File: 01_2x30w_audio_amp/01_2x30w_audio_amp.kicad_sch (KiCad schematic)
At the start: 20 parts, among them J101 CUI 5.08mm, J102 SSQ-107-03-T-D, J103 SSQ-120-03-T-D, J104 CUI 5.08mm, J105 CUI 5.08mm, J108 CUI 5.08mm, J109 CUI 5.08mm, Q101 AON7534, U101 MCP1416

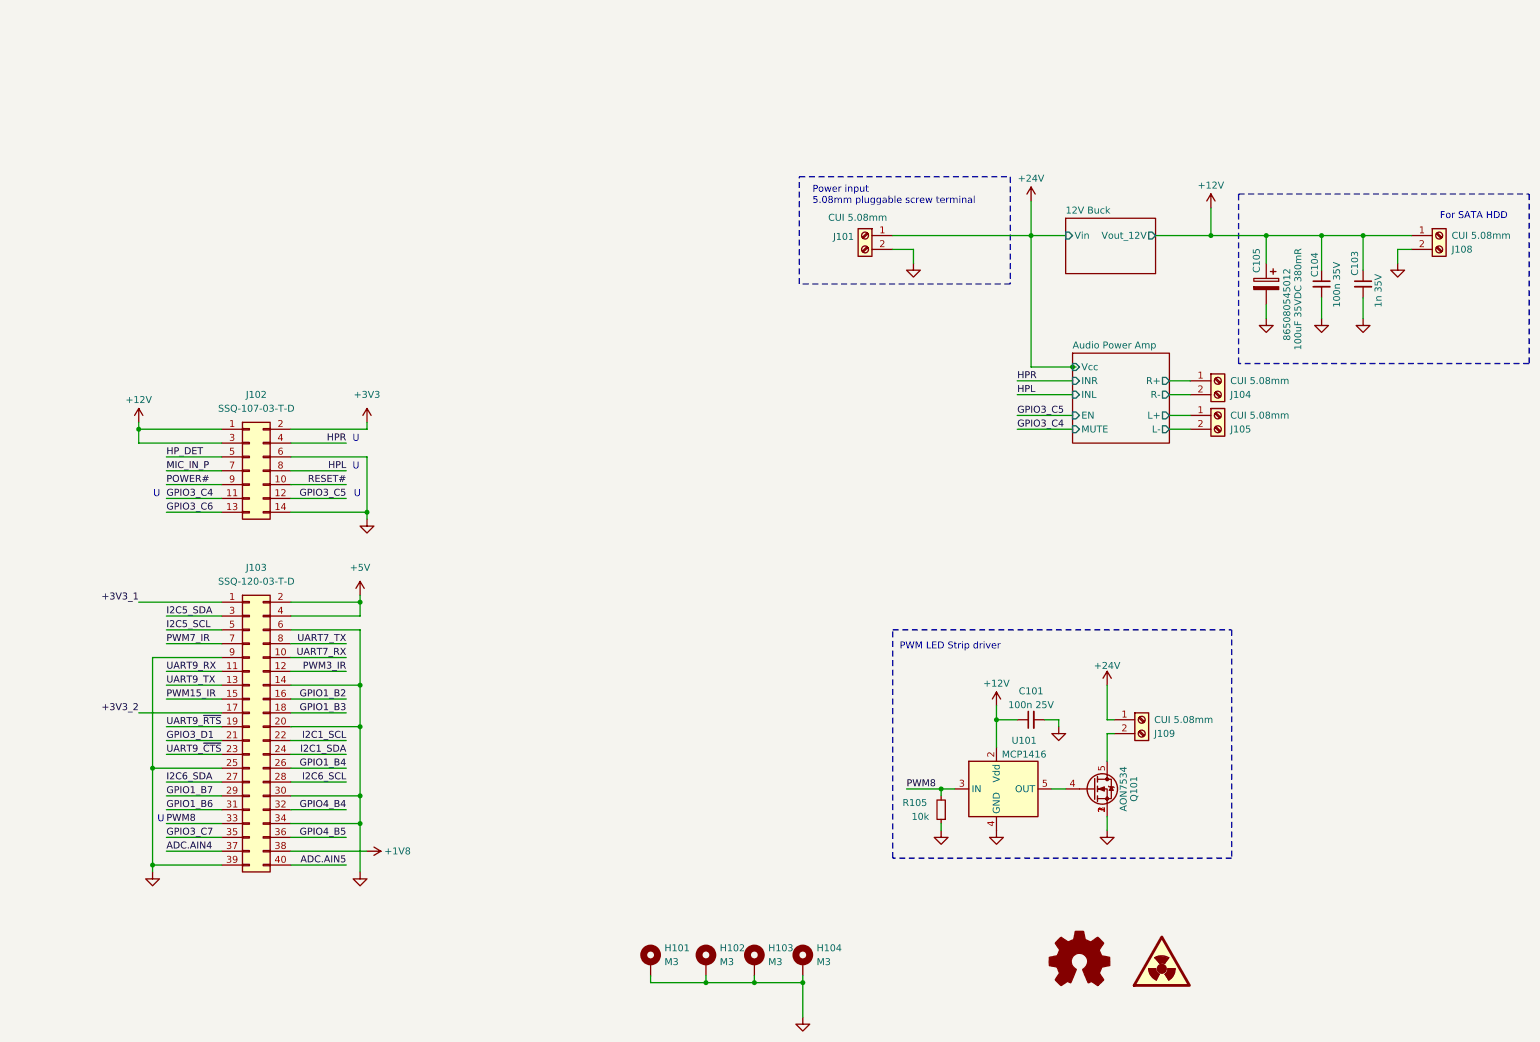
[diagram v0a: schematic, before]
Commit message: Module no. 1 completely redesigned
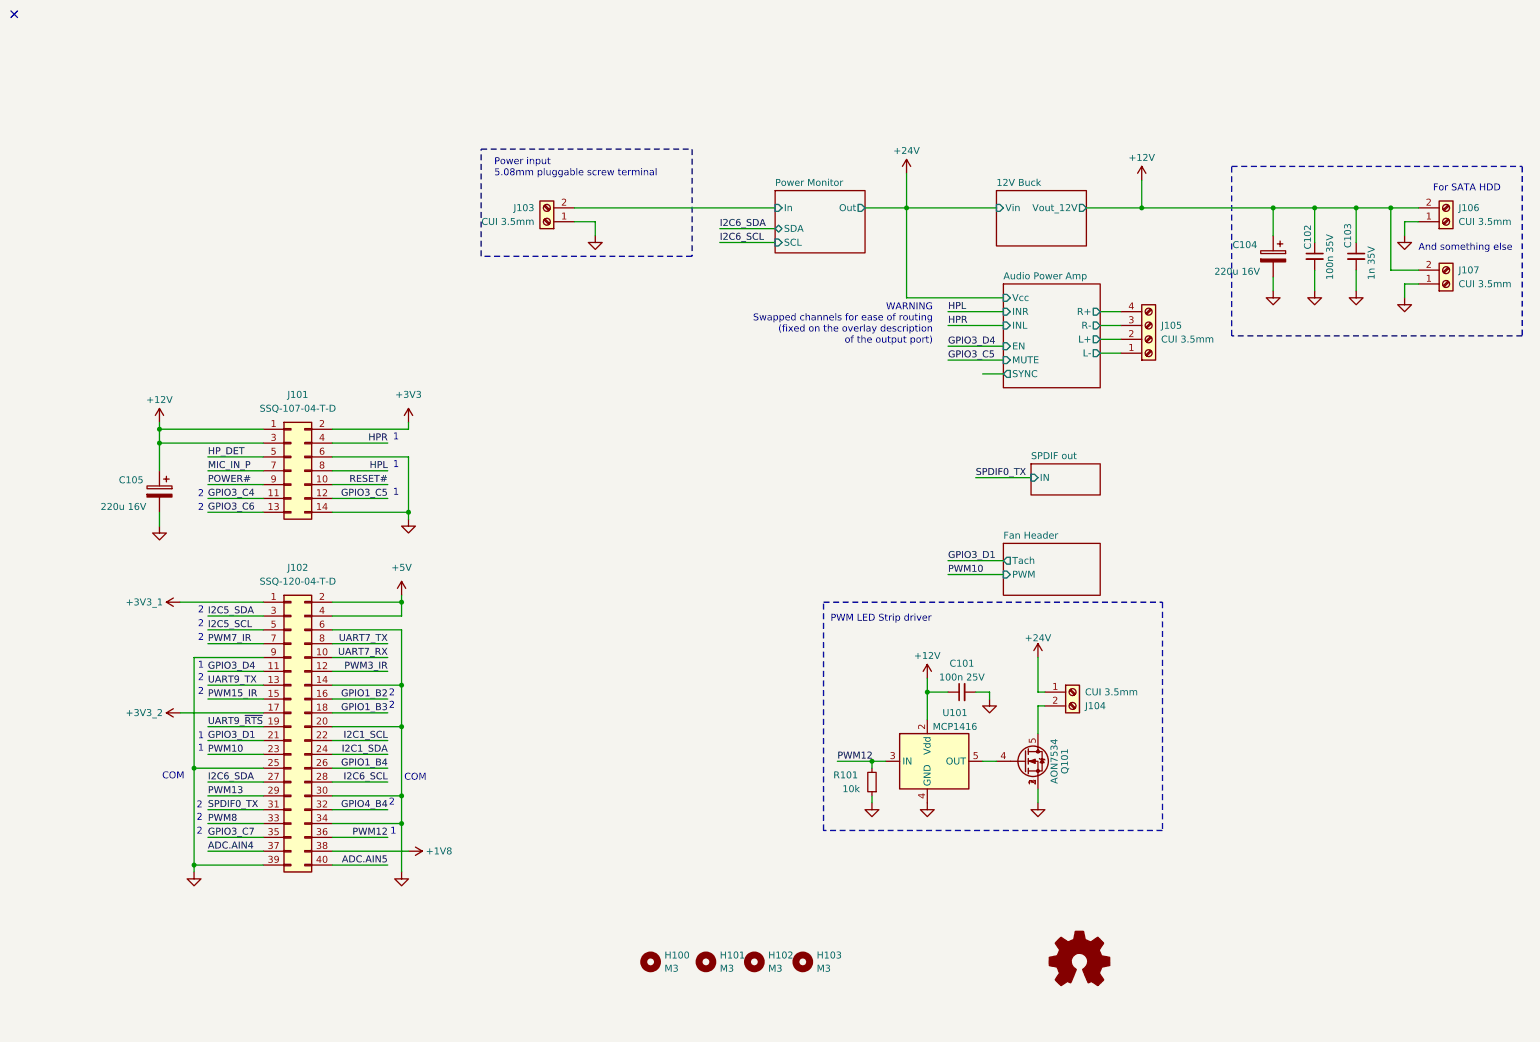
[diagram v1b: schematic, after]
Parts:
- removed J101, J105, J109: CUI 5.08mm, libs:CUI_TBP01R1-508-02BE, symbol Connector:Screw_Terminal_01x02
- removed SYM102: SYM_Radioactive_Large, Symbol:Symbol_Attention_Triangle_8x7mm_Copper, symbol Graphic:SYM_Radioactive_Large
- added C104: A750EK227M1CAAE016, Capacitor_THT:CP_Radial_D6.3mm_P2.50mm, symbol Device:C_Polarized
- added J103, J104, J107: CUI 3.5mm, libs:CUI_TBP03R1-350-02BE, symbol Connector:Screw_Terminal_01x02
- C105: value 865080545012 -> A750EK227M1CAAE016; footprint Capacitor_SMD:C_Elec_6.3x7.7 -> Capacitor_THT:CP_Radial_D6.3mm_P2.50mm
- H100: renamed from H101; footprint MountingHole:MountingHole_3.2mm_M3_DIN965_Pad -> MountingHole:MountingHole_3.2mm_M3_DIN965_Pad_TopBottom; symbol Mechanical:MountingHole_Pad -> Mechanical:MountingHole
- H101: renamed from H102; footprint MountingHole:MountingHole_3.2mm_M3_DIN965_Pad -> MountingHole:MountingHole_3.2mm_M3_DIN965_Pad_TopBottom; symbol Mechanical:MountingHole_Pad -> Mechanical:MountingHole
- H102: renamed from H103; footprint MountingHole:MountingHole_3.2mm_M3_DIN965_Pad -> MountingHole:MountingHole_3.2mm_M3_DIN965_Pad_TopBottom; symbol Mechanical:MountingHole_Pad -> Mechanical:MountingHole
- H103: renamed from H104; footprint MountingHole:MountingHole_3.2mm_M3_DIN965_Pad -> MountingHole:MountingHole_3.2mm_M3_DIN965_Pad_TopBottom; symbol Mechanical:MountingHole_Pad -> Mechanical:MountingHole
- J101: renamed from J102; value SSQ-107-03-T-D -> SSQ-107-04-T-D
- J102: renamed from J103; value SSQ-120-03-T-D -> SSQ-120-04-T-D
- J105: renamed from J104; value CUI 5.08mm -> CUI 3.5mm; footprint libs:CUI_TBP01R1-508-02BE -> libs:CUI_TBP03R1-350-04BE; symbol Connector:Screw_Terminal_01x02 -> Connector:Screw_Terminal_01x04
- J106: renamed from J108; value CUI 5.08mm -> CUI 3.5mm; footprint libs:CUI_TBP01R1-508-02BE -> libs:CUI_TBP03R1-350-02BE
- renumbered C104 to C102, R105 to R101
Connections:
- net +12V: now also J106.2 (Pin_2), C104.1, J107.2 (Pin_2); no longer J106.1 (Pin_1)
- net +24V: now also J104.1 (Pin_1)
- net Audio Power Amp/L+: now also J105.2 (Pin_2)
- net Audio Power Amp/L-: now also J105.1 (Pin_1)
- net Audio Power Amp/R+: now also J105.4 (Pin_4); no longer J105.1 (Pin_1)
- net Audio Power Amp/R-: now also J105.3 (Pin_3); no longer J105.2 (Pin_2)
- net GND: now also J106.1 (Pin_1), C104.2, J103.1 (Pin_1), J107.1 (Pin_1); no longer H100.1, H101.1, H102.1, H103.1, J106.2 (Pin_2)
- net PWM8: no longer R101.2, U101.3 (IN)
- net at Q101.5 (D): now also J104.2 (Pin_2)
- net GPIO1_B6 renamed SPDIF0_TX
- net GPIO1_B7 renamed PWM13
- net GPIO4_B5 renamed PWM12
- net PWM12: now also R101.2, U101.3 (IN)
- net UART9_RX renamed GPIO3_D4
- net UART9_~{CTS} renamed PWM10
- new net Power Monitor/In: J103.2 (Pin_2)
- no-connect marks 0 -> 1
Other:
- added sheet Fan Header (fan_header.kicad_sch)
- added sheet Power Monitor (power_monitor.kicad_sch)
- added sheet SPDIF out (spdif_out.kicad_sch)
- sheet Audio Power Amp ports: added SYNC; removed none
- note added: "1"
- note added: "2"
- note added: "And something else"
- note added: "COM"
- note added: "WARNING Swapped channels for ease of routing (fixed on the overlay description of the output port)"
- note removed: "U"
- moved on the sheet: C101, C102, C103, J101, J102, J106, Q101, R101, U101
